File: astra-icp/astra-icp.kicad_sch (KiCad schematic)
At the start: 70 parts, among them IC1 STM32C011F6P6, J1 PINHD_1x5_Male, SW1 CHOC_HS, SW10 CHOC_HS, SW11 CHOC_HS, SW12 CHOC_HS, SW13 CHOC_HS, SW14 CHOC_HS, SW15 CHOC_HS, SW16 CHOC_HS, SW17 CHOC_HS, SW18 CHOC_HS, SW19 CHOC_HS, SW2 CHOC_HS, SW20 CHOC_HS, SW3 CHOC_HS, SW4 CHOC_HS, SW5 CHOC_HS, SW6 CHOC_HS, SW7 CHOC_HS, SW8 CHOC_HS, SW9 CHOC_HS, U1 PCF8574ATS, U2 PCF8574ATS, U3 MCP251863T-H-SS

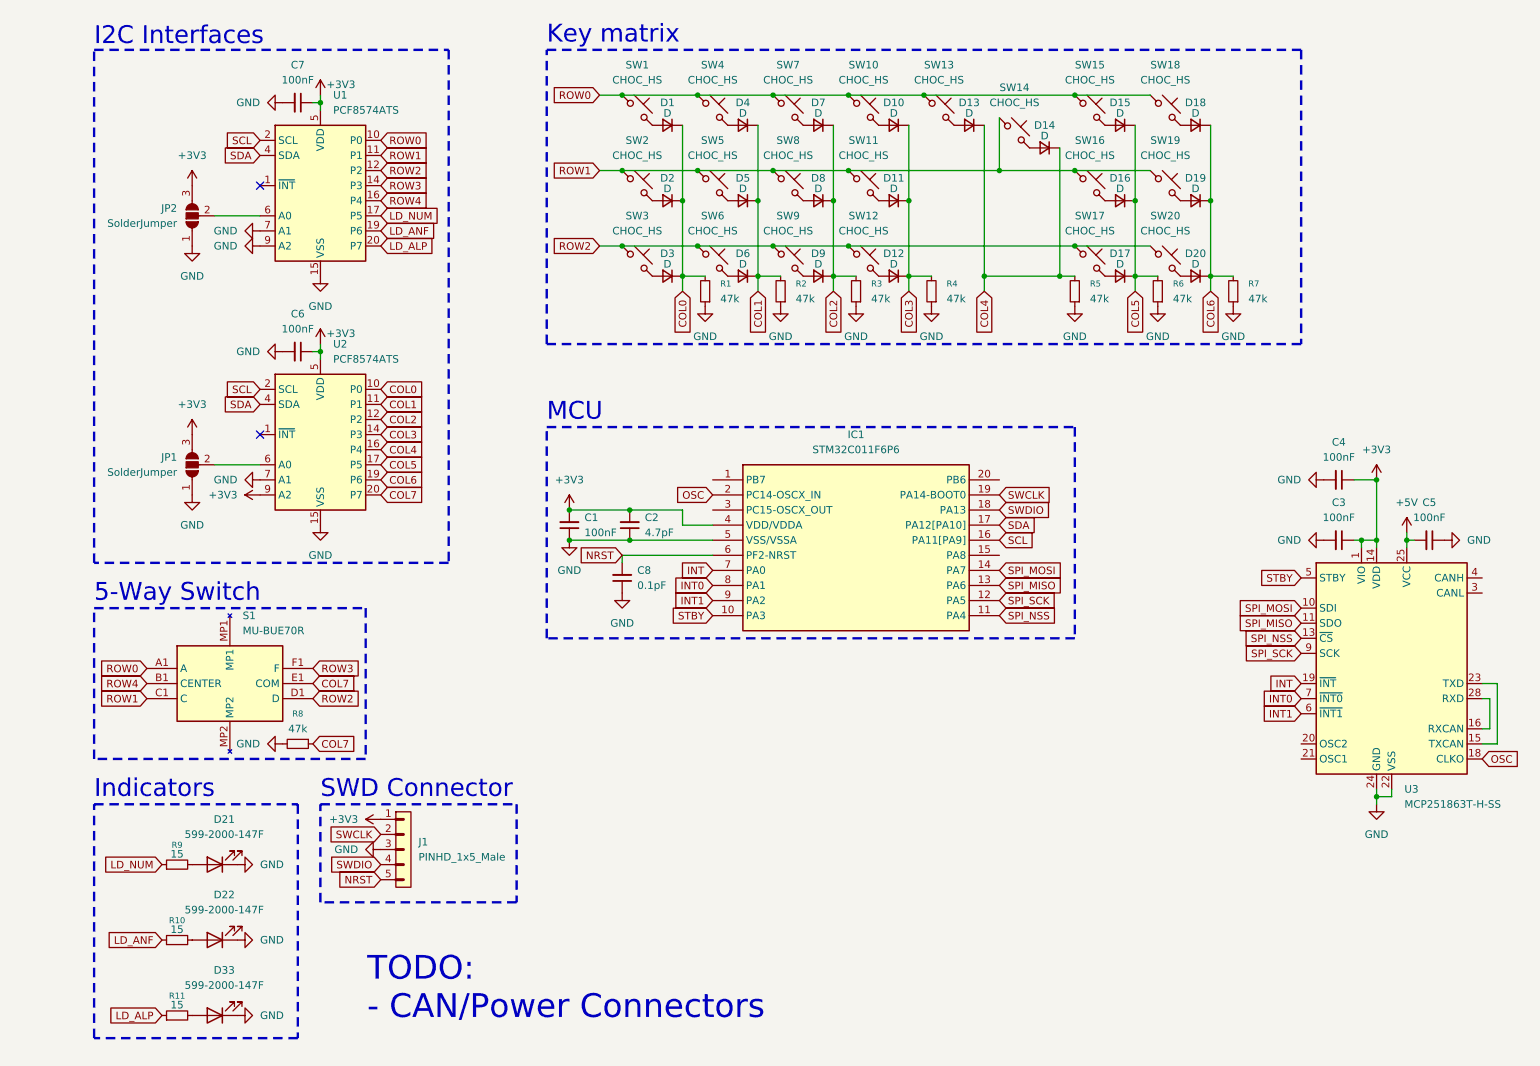
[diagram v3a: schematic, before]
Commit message: feat: Reworked ICP plan
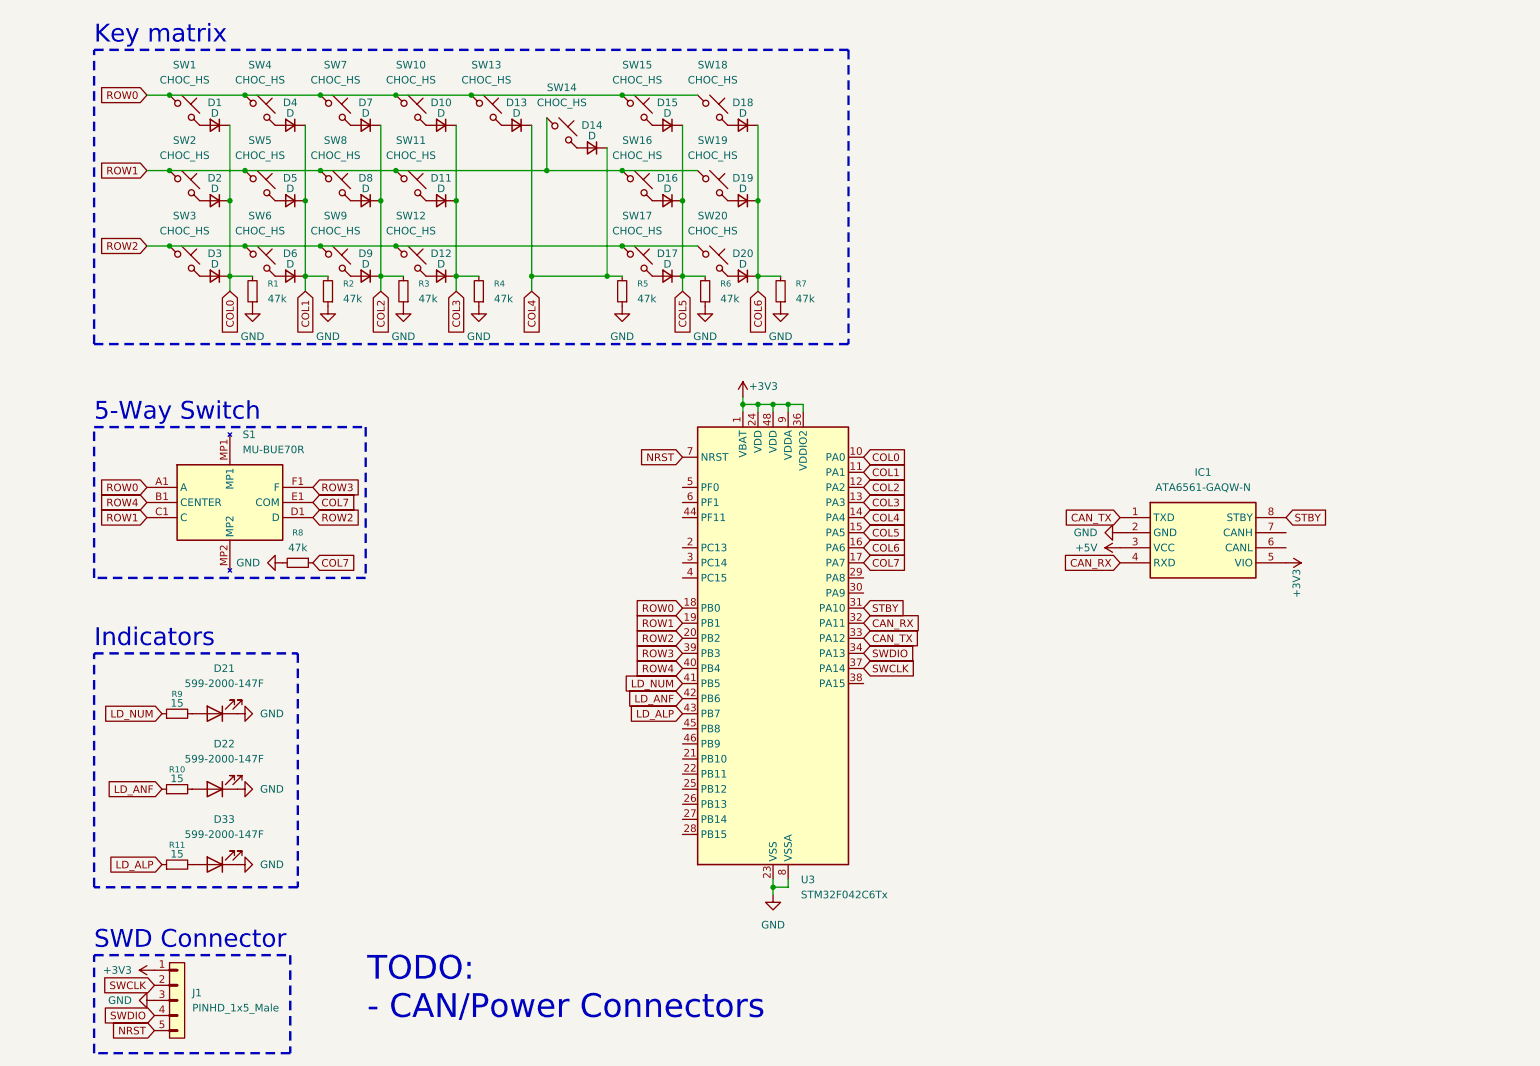
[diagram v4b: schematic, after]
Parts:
- removed C1, C3, C4, C5, C6, C7: 100nF, Capacitor_SMD:C_0805_2012Metric, symbol Device:C_Small
- removed C2: 4.7pF, Capacitor_SMD:C_0805_2012Metric, symbol Device:C_Small
- removed C8: 0.1pF, Capacitor_SMD:C_0805_2012Metric, symbol Device:C_Small
- removed IC1: STM32C011F6P6, footprints:SOP65P640X120-20N, symbol STM32C011F6P6:STM32C011F6P6
- removed JP1, JP2: SolderJumper, Jumper:SolderJumper-3_P2.0mm_Open_TrianglePad1.0x1.5mm, symbol Jumper:SolderJumper_3_Open
- removed U1, U2: PCF8574ATS, Package_SO:SSOP-20_4.4x6.5mm_P0.65mm, symbol Interface_Expansion:PCF8574ATS
- removed U3: MCP251863T-H-SS, Package_SO:SSOP-28_5.3x10.2mm_P0.65mm, symbol Interface_CAN_LIN:MCP251863T-H-SS
- added IC1: ATA6561-GAQW-N, SOIC127P600X175-8N, symbol ATA6561-GAQW-N:ATA6561-GAQW-N
- added U3: STM32F042C6Tx, Package_QFP:LQFP-48_7x7mm_P0.5mm, symbol MCU_ST_STM32F0:STM32F042C6Tx
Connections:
- net +3V3: now also IC1.5 (VIO), U3.1 (VBAT), U3.24 (VDD), U3.36 (VDDIO2), U3.48 (VDD), U3.9 (VDDA)
- net +5V: now also IC1.3 (VCC)
- net COL0: now also U3.10 (PA0)
- net COL1: now also U3.11 (PA1)
- net COL2: now also U3.12 (PA2)
- net COL3: now also U3.13 (PA3)
- net COL4: now also U3.14 (PA4)
- net COL5: now also U3.15 (PA5)
- net COL6: now also U3.16 (PA6)
- net COL7: now also U3.17 (PA7)
- net GND: now also IC1.2 (GND), U3.23 (VSS), U3.35 (VSS), U3.47 (VSS), U3.8 (VSSA)
- net LD_ALP: now also U3.43 (PB7)
- net LD_ANF: now also U3.42 (PB6)
- net LD_NUM: now also U3.41 (PB5)
- net NRST: now also U3.7 (NRST)
- net ROW0: now also U3.18 (PB0)
- net ROW1: now also U3.19 (PB1)
- net ROW2: now also U3.20 (PB2)
- net ROW3: now also U3.39 (PB3)
- net ROW4: now also U3.40 (PB4)
- net STBY: now also IC1.8 (STBY), U3.31 (PA10)
- net SWCLK: now also U3.37 (PA14)
- net SWDIO: now also U3.34 (PA13)
- new net CAN_RX: IC1.4 (RXD), U3.32 (PA11)
- new net CAN_TX: IC1.1 (TXD), U3.33 (PA12)
- no-connect marks 2 -> 0
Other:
- note removed: "I2C Interfaces"
- note removed: "MCU"
- moved on the sheet: D1, D10, D11, D12, D13, D14, D15, D16, D17, D18, D19, D2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

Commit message: feat: Finished ICP schematic
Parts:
- added C1, C2, C3, C4: 100n, Capacitor_SMD:C_0603_1608Metric_Pad1.08x0.95mm_HandSolder, symbol Device:C_Small
- added C5: 4.7p, Capacitor_SMD:C_0603_1608Metric_Pad1.08x0.95mm_HandSolder, symbol Device:C_Small
- added D23: 5V_IND, LED_SMD:LED_0603_1608Metric_Pad1.05x0.95mm_HandSolder, symbol Device:LED
- added D24: 3V3_IND, LED_SMD:LED_0603_1608Metric_Pad1.05x0.95mm_HandSolder, symbol Device:LED
- added J2: PWR_IN, TerminalBlock_Phoenix:TerminalBlock_Phoenix_PT-1,5-3-5.0-H_1x03_P5.00mm_Horizontal, symbol Connector:Screw_Terminal_01x03
- added J3: CAN_TERMINAL, TerminalBlock_Phoenix:TerminalBlock_Phoenix_PT-1,5-2-5.0-H_1x02_P5.00mm_Horizontal, symbol Connector:Screw_Terminal_01x02
- added R12: 120, PCM_Resistor_SMD_AKL:R_0603_1608Metric_Pad1.05x0.95mm_HandSolder, symbol Device:R_Small
- added R13: 145, PCM_Resistor_SMD_AKL:R_0603_1608Metric_Pad1.05x0.95mm_HandSolder, symbol Device:R_Small
- added R14: 60.4, PCM_Resistor_SMD_AKL:R_0603_1608Metric_Pad1.05x0.95mm_HandSolder, symbol Device:R_Small
- D21: value 599-2000-147F -> NUM; Part Number (none) -> 599-2000-147F
- D22: value 599-2000-147F -> ANF; Part Number (none) -> 599-2000-147F
- D33: value 599-2000-147F -> ALP; Part Number (none) -> 599-2000-147F
- U3: value STM32F042C6Tx -> STM32F042C4Tx; Part Number (none) -> STM32F042C4T6
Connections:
- net +3V3: now also C2.1, C3.2, C4.2, C5.2, J2.2 (Pin_2), R14.1
- net +5V: now also C1.1, J2.3 (Pin_3), R13.1
- net GND: now also C1.2, C2.2, C3.1, C4.1, C5.1, D23.1 (K), D24.1 (K), J2.1 (Pin_1)
- net CAN_L: now reaches IC1.6 (CANL)
- net CAN_L: now also J3.1 (Pin_1), R12.2
- net CAN_H: now reaches IC1.7 (CANH)
- net CAN_H: now also J3.2 (Pin_2), R12.1
- new net: D24.2 (A), R14.2
- new net: D23.2 (A), R13.2
- no-connect marks 0 -> 17
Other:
- note added: "CAN Transceiver"
- note added: "MCU"
- note added: "PWR/CAN Connectors"
- note removed: "TODO: - CAN/Power Connectors"
- moved on the sheet: IC1, J1, U3

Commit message: feat: Mostly done ICP PCB
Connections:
- net COL0: now also U3.25 (PB12); no longer U3.10 (PA0)
- net COL1: now also U3.26 (PB13); no longer U3.11 (PA1)
- net COL2: now also U3.27 (PB14); no longer U3.12 (PA2)
- net COL3: now also U3.30 (PA9); no longer U3.13 (PA3)
- net COL4: now also U3.10 (PA0); no longer U3.14 (PA4)
- net COL5: now also U3.11 (PA1); no longer U3.15 (PA5)
- net COL6: now also U3.12 (PA2); no longer U3.16 (PA6)
- net COL7: now also U3.14 (PA4); no longer U3.17 (PA7)
- net LD_ALP: now also U3.22 (PB11); no longer U3.43 (PB7)
- net LD_ANF: now also U3.29 (PA8); no longer U3.42 (PB6)
- net LD_NUM: now also U3.38 (PA15); no longer U3.41 (PB5)
- net ROW0: now also U3.46 (PB9); no longer S1.A1 (A), U3.18 (PB0)
- net ROW3: now also U3.13 (PA3); no longer U3.39 (PB3)
- net ROW4: now also U3.16 (PA6); no longer U3.40 (PB4)
- new net ROW5: S1.A1 (A), U3.15 (PA5)
- no-connect marks 17 -> 16

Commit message: feat: Final work on ICP PCB
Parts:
- added J4: UART, Connector_PinHeader_2.54mm:PinHeader_1x02_P2.54mm_Vertical, symbol PCM_SL_Pin_Headers:PINHD_1x2_Male
- J1: value PINHD_1x5_Male -> SWD
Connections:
- net UART_TX: now reaches U3.42 (PB6)
- net UART_TX: now also J4.1
- net UART_RX: now reaches U3.43 (PB7)
- net UART_RX: now also J4.2
- no-connect marks 16 -> 14
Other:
- note added: "SWD Connectors"
- note removed: "SWD Connector"
- moved on the sheet: J1
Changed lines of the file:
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@@
 	(rectangle
 		(start 165.1 127)
-		(end 198.12 143.51)
+		(end 189.23 149.86)
 		(stroke
 			(width 0.4)
@@
 		)
 	)
-	(text "SWD Connector"
+	(text "SWD Connectors"
 		(exclude_from_sim no)
 		(at 165.1 124.46 0)
@@
 	)
 	(no_connect
-		(at 176.53 81.28)
+		(at 176.53 73.66)
 	)
 	(no_connect
@@
 	)
 	(no_connect
-		(at 176.53 78.74)
+		(at 176.53 86.36)
 	)
 	(no_connect
-		(at 176.53 58.42)
+		(at 176.53 78.74)
 	)
 	(no_connect
-		(at 176.53 83.82)
+		(at 176.53 58.42)
 	)
 	(no_connect
@@
 	)
 	(no_connect
-		(at 176.53 104.14)
-	)
-	(no_connect
-		(at 176.53 73.66)
+		(at 176.53 76.2)
 	)
 	(no_connect
-		(at 176.53 76.2)
+		(at 176.53 104.14)
 	)
 	(no_connect
@@
 		(at 176.53 60.96)
 	)
-	(no_connect
-		(at 176.53 86.36)
-	)
 	(wire
 		(pts
@@
 		)
 	)
+	(global_label "UART_TX"
+		(shape input)
+		(at 176.53 81.28 180)
+		(fields_autoplaced yes)
+		(effects
+			(font
+				(size 1.27 1.27)
+			)
+			(justify right)
+		)
+		(property "Intersheetrefs" "${INTERSHEET_REFS}"
+			(at 165.7434 81.28 0)
+			(effects
+				(font
+					(size 1.27 1.27)
+				)
+				(justify right)
+				(hide yes)
+			)
+		)
+	)
 	(global_label "SWDIO"
 		(shape input)
@@
 	(global_label "NRST"
 		(shape input)
-		(at 175.26 139.7 180)
+		(at 176.53 139.7 180)
 		(fields_autoplaced yes)
 		(effects
@@
 		)
 		(property "Intersheetrefs" "${INTERSHEET_REFS}"
-			(at 167.4972 139.7 0)
+			(at 168.7672 139.7 0)
 			(effects
 				(font
@@
 		)
 	)
+	(global_label "UART_TX"
+		(shape input)
+		(at 176.53 144.78 180)
+		(fields_autoplaced yes)
+		(effects
+			(font
+				(size 1.27 1.27)
+			)
+			(justify right)
+		)
+		(property "Intersheetrefs" "${INTERSHEET_REFS}"
+			(at 165.7434 144.78 0)
+			(effects
+				(font
+					(size 1.27 1.27)
+				)
+				(justify right)
+				(hide yes)
+			)
+		)
+	)
 	(global_label "SWCLK"
 		(shape input)
@@
 	(global_label "SWCLK"
 		(shape input)
-		(at 175.26 132.08 180)
+		(at 176.53 132.08 180)
 		(fields_autoplaced yes)
 		(effects
@@
 		)
 		(property "Intersheetrefs" "${INTERSHEET_REFS}"
-			(at 166.0458 132.08 0)
+			(at 167.3158 132.08 0)
 			(effects
 				(font
@@
 		)
 	)
+	(global_label "UART_RX"
+		(shape input)
+		(at 176.53 147.32 180)
+		(fields_autoplaced yes)
+		(effects
+			(font
+				(size 1.27 1.27)
+			)
+			(justify right)
+		)
+		(property "Intersheetrefs" "${INTERSHEET_REFS}"
+			(at 165.441 147.32 0)
+			(effects
+				(font
+					(size 1.27 1.27)
+				)
+				(justify right)
+				(hide yes)
+			)
+		)
+	)
 	(global_label "ROW5"
 		(shape input)
@@
 		)
 	)
+	(global_label "UART_RX"
+		(shape input)
+		(at 176.53 83.82 180)
+		(fields_autoplaced yes)
+		(effects
+			(font
+				(size 1.27 1.27)
+			)
+			(justify right)
+		)
+		(property "Intersheetrefs" "${INTERSHEET_REFS}"
+			(at 165.441 83.82 0)
+			(effects
+				(font
+					(size 1.27 1.27)
+				)
+				(justify right)
+				(hide yes)
+			)
+		)
+	)
 	(global_label "LD_NUM"
 		(shape input)
@@
 	(global_label "SWDIO"
 		(shape input)
-		(at 175.26 137.16 180)
+		(at 176.53 137.16 180)
 		(fields_autoplaced yes)
 		(effects
@@
 		)
 		(property "Intersheetrefs" "${INTERSHEET_REFS}"
-			(at 166.4086 137.16 0)
+			(at 167.6786 137.16 0)
 			(effects
 				(font
@@
 	(symbol
 		(lib_id "power:+3V3")
-		(at 175.26 129.54 90)
+		(at 176.53 129.54 90)
 		(unit 1)
 		(exclude_from_sim no)
@@
 		(fields_autoplaced yes)
 		(property "Reference" "#PWR034"
-			(at 179.07 129.54 0)
+			(at 180.34 129.54 0)
 			(effects
 				(font
@@
 		)
 		(property "Value" "+3V3"
-			(at 171.45 129.5399 90)
+			(at 172.72 129.5399 90)
 			(effects
 				(font
@@
 		)
 		(property "Footprint" ""
-			(at 175.26 129.54 0)
+			(at 176.53 129.54 0)
 			(effects
 				(font
@@
 		)
 		(property "Datasheet" ""
-			(at 175.26 129.54 0)
+			(at 176.53 129.54 0)
 			(effects
 				(font
@@
 		)
 		(property "Description" "Power symbol creates a global label with name \"+3V3\""
-			(at 175.26 129.54 0)
+			(at 176.53 129.54 0)
 			(effects
 				(font
@@
 	(symbol
 		(lib_id "PCM_SL_Pin_Headers:PINHD_1x5_Male")
-		(at 179.07 134.62 0)
+		(at 180.34 134.62 0)
 		(unit 1)
 		(exclude_from_sim no)
@@
 		(fields_autoplaced yes)
 		(property "Reference" "J1"
-			(at 181.61 133.3499 0)
+			(at 182.88 133.3499 0)
 			(effects
 				(font
@@
 			)
 		)
-		(property "Value" "PINHD_1x5_Male"
-			(at 181.61 135.8899 0)
+		(property "Value" "SWD"
+			(at 182.88 135.8899 0)
 			(effects
 				(font
@@
 		)
 		(property "Footprint" "Connector_PinHeader_2.54mm:PinHeader_1x05_P2.54mm_Vertical"
-			(at 177.8 121.92 0)
+			(at 179.07 121.92 0)
 			(effects
 				(font
@@
 		)
 		(property "Datasheet" ""
-			(at 179.07 123.19 0)
+			(at 180.34 123.19 0)
 			(effects
 				(font
@@
 		)
 		(property "Description" "Pin Header male with pin space 2.54mm. Pin Count -5"
-			(at 179.07 134.62 0)
+			(at 180.34 134.62 0)
 			(effects
 				(font
@@
 	)
 	(symbol
+		(lib_id "PCM_SL_Pin_Headers:PINHD_1x2_Male")
+		(at 180.34 146.05 0)
+		(unit 1)
+		(exclude_from_sim no)
+		(in_bom yes)
+		(on_board yes)
+		(dnp no)
+		(fields_autoplaced yes)
+		(property "Reference" "J4"
+			(at 182.88 144.7799 0)
+			(effects
+				(font
+					(size 1.27 1.27)
+				)
+				(justify left)
+			)
+		)
+		(property "Value" "UART"
+			(at 182.88 147.3199 0)
+			(effects
+				(font
+					(size 1.27 1.27)
+				)
+				(justify left)
+			)
+		)
+		(property "Footprint" "Connector_PinHeader_2.54mm:PinHeader_1x02_P2.54mm_Vertical"
+			(at 181.61 149.86 0)
+			(effects
+				(font
+					(size 1.27 1.27)
+				)
+				(hide yes)
+			)
+		)
+		(property "Datasheet" ""
+			(at 180.34 138.43 0)
+			(effects
+				(font
+					(size 1.27 1.27)
+				)
+				(hide yes)
+			)
+		)
+		(property "Description" "Pin Header male with pin space 2.54mm. Pin Count -2"
+			(at 180.34 146.05 0)
+			(effects
+				(font
+					(size 1.27 1.27)
+				)
+				(hide yes)
+			)
+		)
+		(pin "1"
+		)
+		(pin "2"
+		)
+		(instances
+			(project ""
+				(path "/2c0b7f62-c984-4395-ba2f-356f19f7f2d0"
+					(reference "J4")
+					(unit 1)
+				)
+			)
+		)
+	)
+	(symbol
 		(lib_id "power:+5V")
 		(at 36.83 173.99 90)
@@
 	(symbol
 		(lib_id "power:GND")
-		(at 175.26 134.62 270)
+		(at 176.53 134.62 270)
 		(unit 1)
 		(exclude_from_sim no)
@@
 		(fields_autoplaced yes)
 		(property "Reference" "#PWR035"
-			(at 168.91 134.62 0)
+			(at 170.18 134.62 0)
 			(effects
 				(font
@@
 		)
 		(property "Value" "GND"
-			(at 171.45 134.6199 90)
+			(at 172.72 134.6199 90)
 			(effects
 				(font
@@
 		)
 		(property "Footprint" ""
-			(at 175.26 134.62 0)
+			(at 176.53 134.62 0)
 			(effects
 				(font
@@
 		)
 		(property "Datasheet" ""
-			(at 175.26 134.62 0)
+			(at 176.53 134.62 0)
 			(effects
 				(font
@@
 		)
 		(property "Description" "Power symbol creates a global label with name \"GND\" , ground"
-			(at 175.26 134.62 0)
+			(at 176.53 134.62 0)
 			(effects
 				(font

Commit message: feat: Changed resistors to 0603
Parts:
- R1, R10, R11, R2, R3, R4, R5, R6, R7, R8, R9: footprint PCM_Resistor_SMD_AKL:R_0201_0603Metric_Pad0.64x0.40mm_HandSolder -> PCM_Resistor_SMD_AKL:R_0603_1608Metric_Pad1.05x0.95mm_HandSolder
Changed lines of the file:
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@@
 			)
 		)
-		(property "Footprint" "PCM_Resistor_SMD_AKL:R_0201_0603Metric_Pad0.64x0.40mm_HandSolder"
+		(property "Footprint" "PCM_Resistor_SMD_AKL:R_0603_1608Metric_Pad1.05x0.95mm_HandSolder"
 			(at 64.77 66.04 0)
 			(effects
@@
 			)
 		)
-		(property "Footprint" "PCM_Resistor_SMD_AKL:R_0201_0603Metric_Pad0.64x0.40mm_HandSolder"
+		(property "Footprint" "PCM_Resistor_SMD_AKL:R_0603_1608Metric_Pad1.05x0.95mm_HandSolder"
 			(at 128.27 66.04 0)
 			(effects
@@
 			)
 		)
-		(property "Footprint" "PCM_Resistor_SMD_AKL:R_0201_0603Metric_Pad0.64x0.40mm_HandSolder"
+		(property "Footprint" "PCM_Resistor_SMD_AKL:R_0603_1608Metric_Pad1.05x0.95mm_HandSolder"
 			(at 39.37 162.56 0)
 			(effects
@@
 			)
 		)
-		(property "Footprint" "PCM_Resistor_SMD_AKL:R_0201_0603Metric_Pad0.64x0.40mm_HandSolder"
+		(property "Footprint" "PCM_Resistor_SMD_AKL:R_0603_1608Metric_Pad1.05x0.95mm_HandSolder"
 			(at 140.97 66.04 0)
 			(effects
@@
 			)
 		)
-		(property "Footprint" "PCM_Resistor_SMD_AKL:R_0201_0603Metric_Pad0.64x0.40mm_HandSolder"
+		(property "Footprint" "PCM_Resistor_SMD_AKL:R_0603_1608Metric_Pad1.05x0.95mm_HandSolder"
 			(at 59.69 111.76 0)
 			(effects
@@
 			)
 		)
-		(property "Footprint" "PCM_Resistor_SMD_AKL:R_0201_0603Metric_Pad0.64x0.40mm_HandSolder"
+		(property "Footprint" "PCM_Resistor_SMD_AKL:R_0603_1608Metric_Pad1.05x0.95mm_HandSolder"
 			(at 114.3 66.04 0)
 			(effects
@@
 			)
 		)
-		(property "Footprint" "PCM_Resistor_SMD_AKL:R_0201_0603Metric_Pad0.64x0.40mm_HandSolder"
+		(property "Footprint" "PCM_Resistor_SMD_AKL:R_0603_1608Metric_Pad1.05x0.95mm_HandSolder"
 			(at 39.37 137.16 0)
 			(effects
@@
 			)
 		)
-		(property "Footprint" "PCM_Resistor_SMD_AKL:R_0201_0603Metric_Pad0.64x0.40mm_HandSolder"
+		(property "Footprint" "PCM_Resistor_SMD_AKL:R_0603_1608Metric_Pad1.05x0.95mm_HandSolder"
 			(at 77.47 66.04 0)
 			(effects
@@
 			)
 		)
-		(property "Footprint" "PCM_Resistor_SMD_AKL:R_0201_0603Metric_Pad0.64x0.40mm_HandSolder"
+		(property "Footprint" "PCM_Resistor_SMD_AKL:R_0603_1608Metric_Pad1.05x0.95mm_HandSolder"
 			(at 39.37 149.86 0)
 			(effects
@@
 			)
 		)
-		(property "Footprint" "PCM_Resistor_SMD_AKL:R_0201_0603Metric_Pad0.64x0.40mm_HandSolder"
+		(property "Footprint" "PCM_Resistor_SMD_AKL:R_0603_1608Metric_Pad1.05x0.95mm_HandSolder"
 			(at 52.07 66.04 0)
 			(effects
@@
 			)
 		)
-		(property "Footprint" "PCM_Resistor_SMD_AKL:R_0201_0603Metric_Pad0.64x0.40mm_HandSolder"
+		(property "Footprint" "PCM_Resistor_SMD_AKL:R_0603_1608Metric_Pad1.05x0.95mm_HandSolder"
 			(at 90.17 66.04 0)
 			(effects
